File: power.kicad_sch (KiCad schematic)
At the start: 41 parts, among them J16 PJ-037A, Q1 AOSS21115C, Q2 AOSS21115C, Q3 DSS20200L-7, U17 TPS82085SILT, U19 AP7361C-33FGE-7, U26 TPS82084SILT, U27 LP5912-1.2DRVR, U28 LP5912-1.8DRVR, U29 LP5912-1.8DRVR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

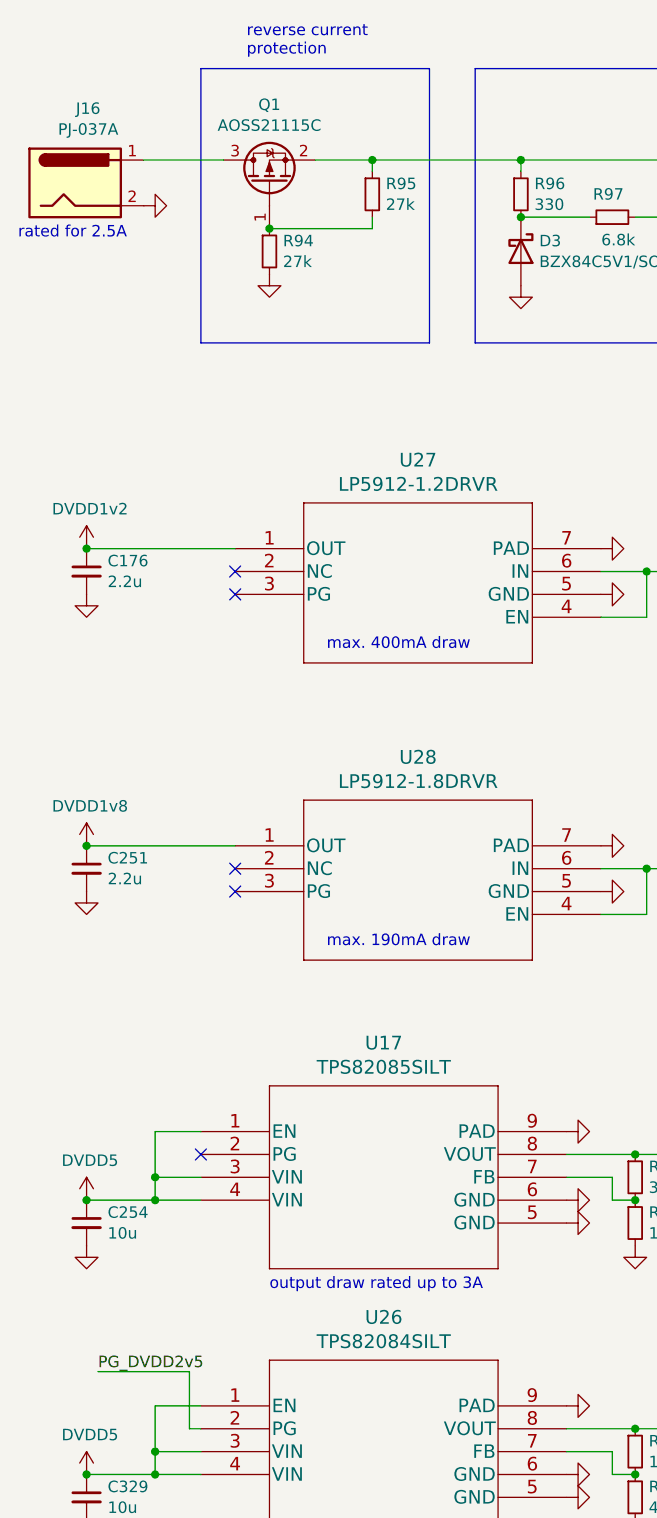
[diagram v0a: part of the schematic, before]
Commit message: update schematic to v1.5
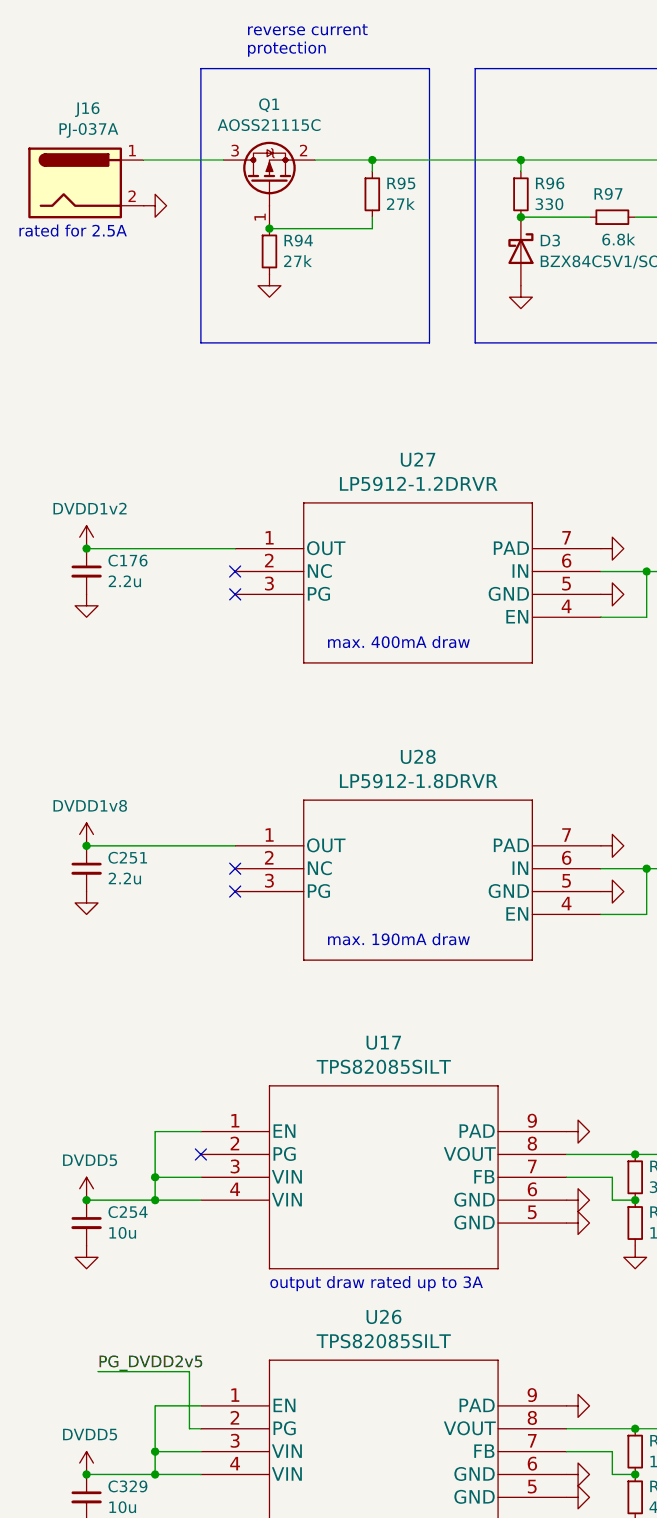
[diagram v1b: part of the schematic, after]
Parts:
- U26: value TPS82084SILT -> TPS82085SILT

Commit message: update schematic to v1.6
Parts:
- D3: footprint Diode_SMD:D_SOT-23_ANK -> Diode_SMD:D_SOD-323
